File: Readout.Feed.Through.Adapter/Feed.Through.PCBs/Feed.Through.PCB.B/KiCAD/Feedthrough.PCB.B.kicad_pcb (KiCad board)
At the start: 2 copper layers, 68 x 68 mm, 20 parts

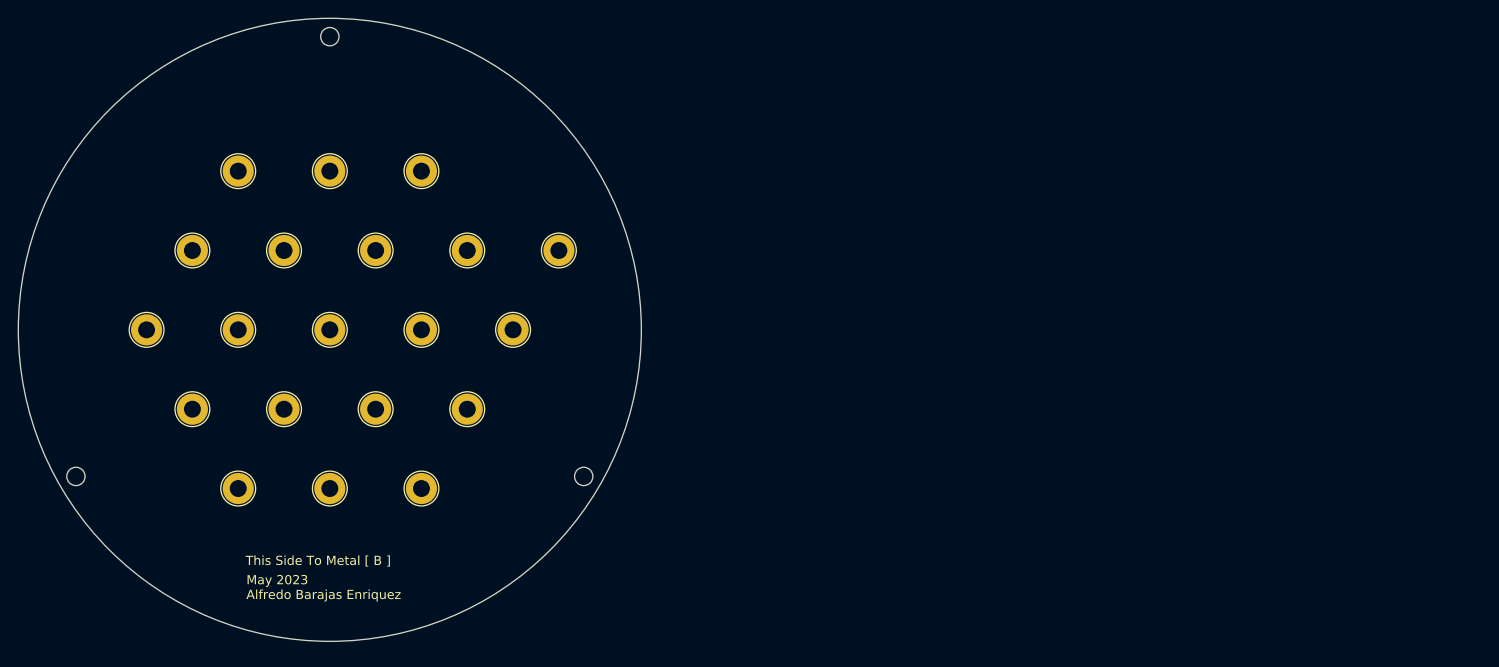
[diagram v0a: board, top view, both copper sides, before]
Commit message: Updated ReadoutPCBs to allow smoother gasflow
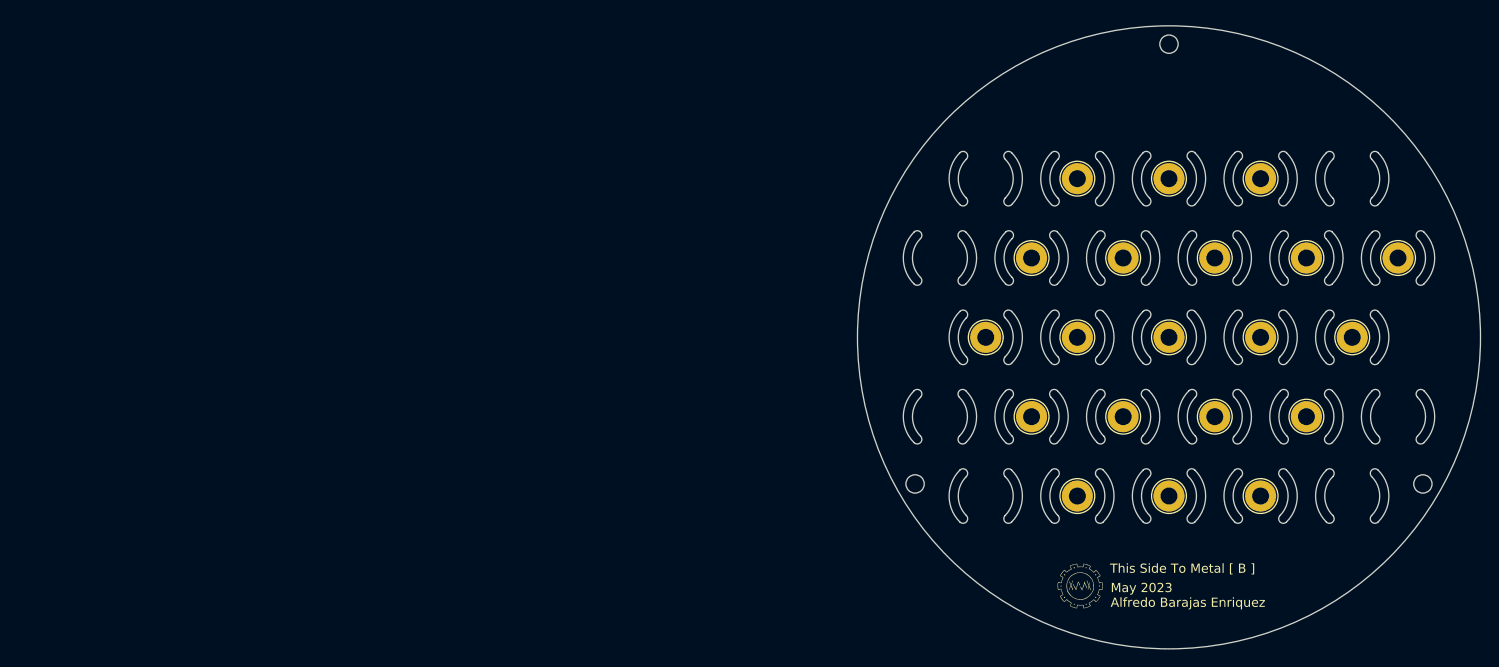
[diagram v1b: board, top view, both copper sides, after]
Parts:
- added G***: LOGO, LOGO, F.Cu at (135.5, 81.0)
- moved CH1 91.6 mm to (125.2, 53.9)
- moved CH1 91.6 mm to (130.2, 62.5)
- moved CH1 91.6 mm to (135.2, 36.6)
- moved CH1 91.6 mm to (135.2, 71.2)
- moved CH1 91.6 mm to (130.2, 45.2)
- moved CH10 91.6 mm to (155.2, 53.9)
- moved CH11 91.6 mm to (165.2, 53.9)
- moved CH12 91.6 mm to (140.2, 62.5)
- moved CH13 91.6 mm to (150.2, 62.5)
- moved CH14 91.6 mm to (160.2, 62.5)
- moved CH15 91.6 mm to (145.2, 71.2)
- moved CH16 91.6 mm to (155.2, 71.2)
- moved CH2 91.6 mm to (145.2, 36.6)
- moved CH3 91.6 mm to (155.2, 36.6)
- moved CH4 91.6 mm to (140.2, 45.2)
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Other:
- outline, holes or cut-outs redrawn
